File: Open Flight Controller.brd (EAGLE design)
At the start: 45.5 x 37 mm, 74 parts, among them IC1 TPS62133RGTT, IC2 LDL112PU33R, IC3 ICM-20689-V2.2, IC4 AK8963N, IC5 BMP280, IC6 STM32F765VGT6, Q1 IRLML6244TRPBF, Q2 SDTC114EET1G, X1 DM3BT-DSF-PEJS, X2 0473460001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

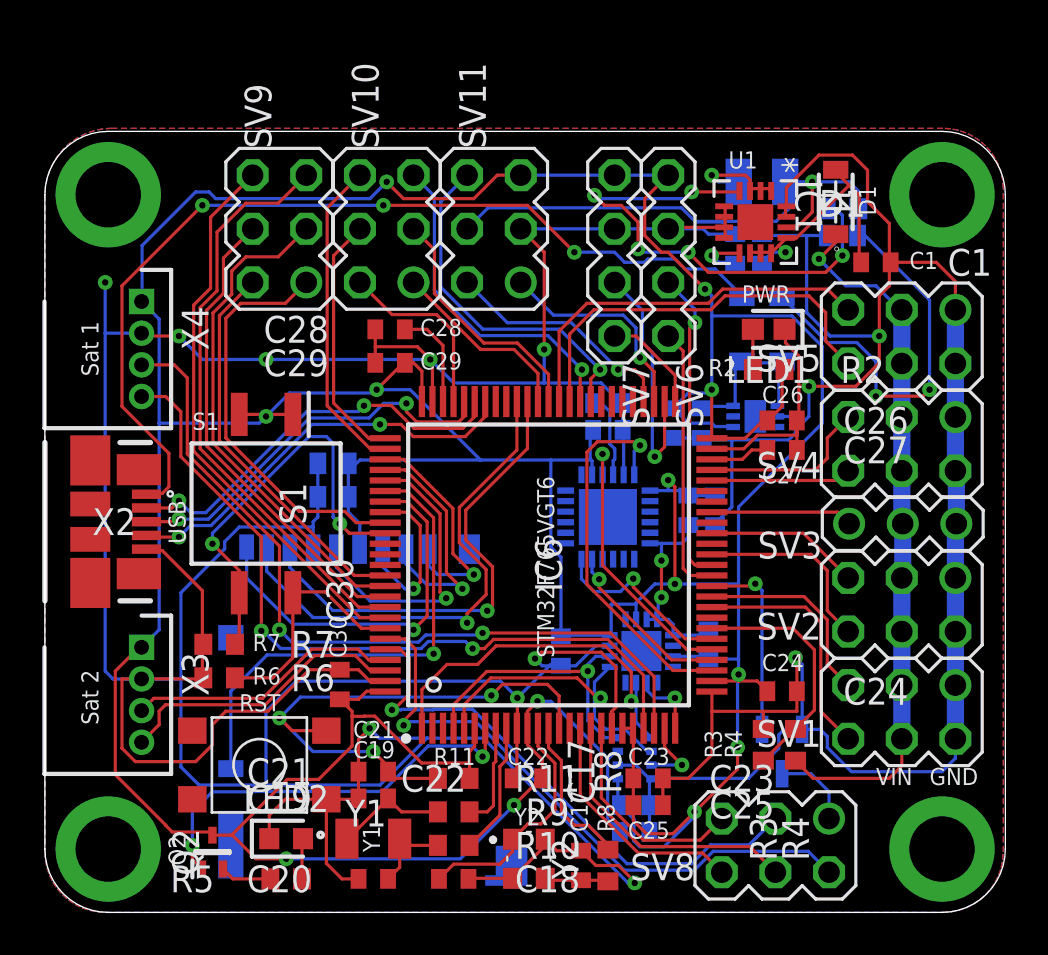
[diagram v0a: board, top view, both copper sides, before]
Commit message: Added reset-pin and pwm-led
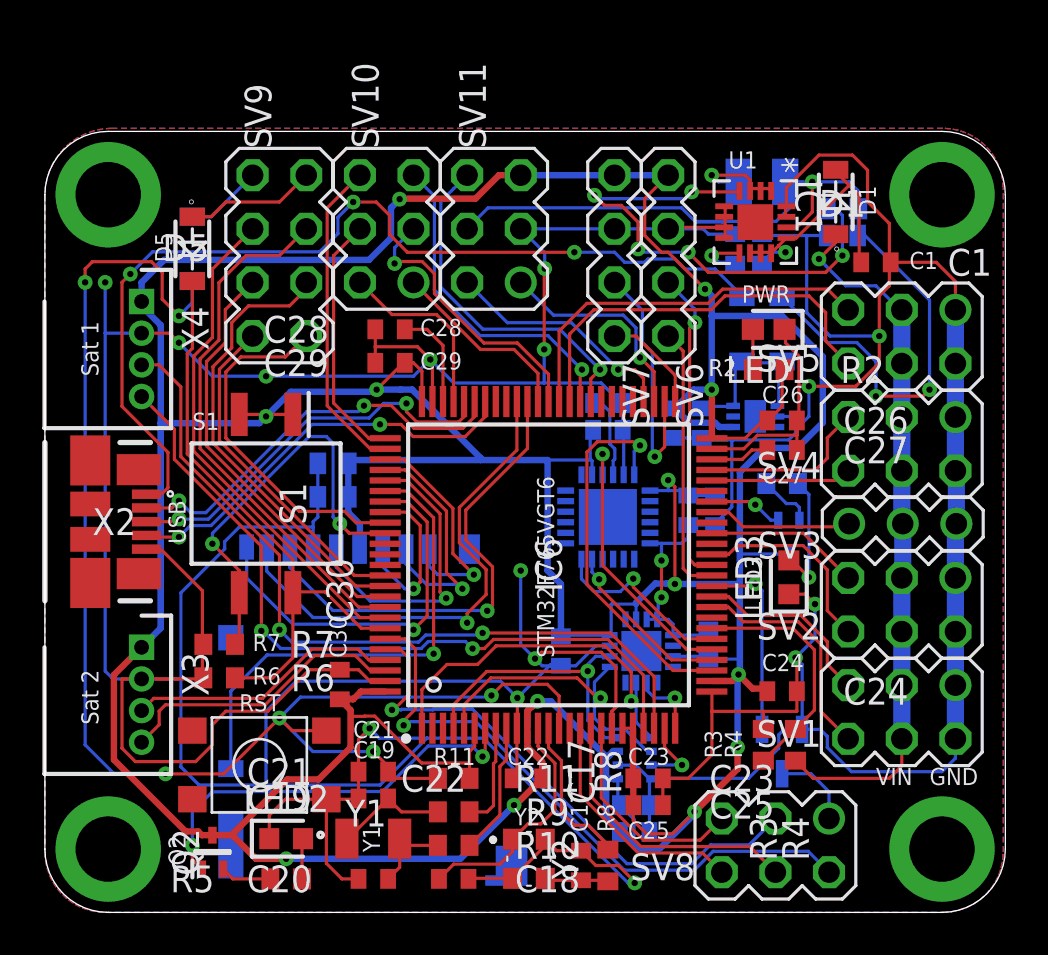
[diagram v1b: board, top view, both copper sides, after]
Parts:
- added D4, D5: (no value), RBR3MM40ATR:PMDU
- added LED3: BLUE, VLMB1300-GS08:LEDC1608X100N
- added Q3: SDTC114EET1G, SDTC114EET1G:SOT50P160X90-3N
- added R12: 1k, CRCW06031K00FKEA:RESC1608X50N
- SV9: value MA03-2 -> (none); device MA03-2:MA03-2 -> MA04-2:MA04-2
- moved SV9 1.27 mm to (11.1, 31.1)
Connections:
- net GPIO2(P+T_CS) renamed GPIO2
- new net BOOT_PIN: D5.1, SV9.7
- new net N$17: Q3.2, R12.2
- new net N$20: LED3.2, R12.1
- new net RST_PIN: D4.1, SV9.8
- net !RST: now also D4.2
- net 3.3V: now also Q3.3
- net BOOT: now also D5.2
- net GND: now also LED3.1
- net PWM14/LCD_CLK: now also Q3.1
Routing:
- net !RST: track 27.0 -> 68.7 mm, vias 3 -> 6
- net 3.3V: track 260.5 -> 294.6 mm
- net BOOT: track 11.9 -> 28.8 mm
- net GND: track 351.0 -> 360.4 mm, vias 14 -> 17
- net BOOT_PIN: track 0.00 -> 6.21 mm
- net N$20: track 0.00 -> 5.94 mm, vias 0 -> 1
- net RST_PIN: track 0.00 -> 3.67 mm
- net PWM14/LCD_CLK: track 0.00 -> 3.51 mm, vias 0 -> 1
- net N$17: track 0.00 -> 2.64 mm
- net SPI2_SCK: track 19.4 -> 16.9 mm
- net PWM42/I2C1_SDA/I2C4_SDA: track 26.6 -> 24.0 mm
- net PWM32/SPI3,6_MOSI: track 22.6 -> 20.1 mm
- net JTDO/SPI3,6_SCK: track 18.6 -> 16.1 mm
- net PWM41/I2C1_SCL/I2C4_SCL: track 27.8 -> 25.3 mm
- net NJTRST/SPI3,6_MISO: track 23.8 -> 21.5 mm
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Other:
- board text added: "D4"
- board text added: "D5"
- board text added: "LED3"
- board text added: "Not CE / FCC approved"
- board text added: "Q3"
- board text added: "R12"
- board text removed: "Not FCC/CE approved"
